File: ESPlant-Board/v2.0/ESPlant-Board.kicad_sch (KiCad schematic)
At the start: 32 parts, among them J1 Conn_02x04_Counter_Clockwise, U1 ESP32-S2-MINI-1-N4, U2 BH-AAA-B5AK001, U3 Reset, U4 Boot, U5 Temp/Humid-Sensor, U6 Light sensor, U7 AMS1117-3_3, U8 MK-12C02-G025

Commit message: Board: Update panel
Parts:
- removed J1: Conn_02x04_Counter_Clockwise, Connector_PinHeader_2.54mm:PinHeader_2x04_P2.54mm_Vertical, symbol Connector_Generic:Conn_02x04_Odd_Even
- removed R5: 10k, Resistor_SMD:R_0402_1005Metric, symbol Device:R
- removed R7: 1M, Resistor_SMD:R_0402_1005Metric, symbol Device:R
- removed U2: BH-AAA-B5AK001, CustomFootprints:BAT-SMD_BH-AAA-B5AA001, symbol Custom_Parts:BH-AAA-B5AK001
- added J1: Conn_01x05, Connector_PinHeader_2.54mm:PinHeader_1x05_P2.54mm_Vertical, symbol Connector_Generic:Conn_01x05
- added U9: ~, CustomFootprints:AAA Battery-spring, symbol Custom_Parts:AAA_Battery-Spring
- C3: value 1uF -> 150pF; LCSC C52923 -> C1527; MPN C52923 -> C1527
- USB1: now in the parts list
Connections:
- net Voltage_Measurement_Select_1 is gone; now on net TH_SCL: U1.35 (IO39)
- net +3V3: now also J1.5 (Pin_5)
- net GND: now also J1.1 (Pin_1), U9.1 (-)
- net IO0: now also J1.4 (Pin_4)
- net LED_GREEN: now also U1.38 (IO42); no longer U1.20 (IO16)
- net LED_RED: now also U1.37 (IO41); no longer U1.21 (IO17)
- net Light_Sensor_Analog: now also U1.7 (IO3); no longer U1.8 (IO4)
- net Light_Sensor_In: now also U1.36 (IO40); no longer U1.32 (IO36)
- net Light_Sensor_Select_1: now also U1.32 (IO36); no longer U1.33 (IO37)
- net RX: now also J1.2 (Pin_2)
- net Square_Wave_Signal: now also U1.21 (IO17); no longer U1.29 (IO34)
- net TH_SCL: no longer U1.38 (IO42)
- net TH_SDA: now also U1.34 (IO38); no longer U1.37 (IO41)
- net TX: now also J1.3 (Pin_3)
- net Voltage_Measurement_Analog: now also U1.10 (IO6); no longer U1.7 (IO3)
- net at U8.3: now also U9.2 (+)
- net IO2: no longer names the net of U1.6 (IO2)
- net Voltage_Measurement_Select_2 renamed Voltage_Measurement_Select
- net Voltage_Measurement_Select: now also U1.20 (IO16); no longer U1.34 (IO38)
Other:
- note removed: "10k is best for a ~6 Mhz Signal max(3.3*(1-e^(-(1/x)/(10000*7*10^-12))) -3.3*(1-e^(-(1/x)/(10000*47*10^-12)))) Expecting a sensor capacitance between 7 pF and 47 pF"
- moved on the sheet: R6

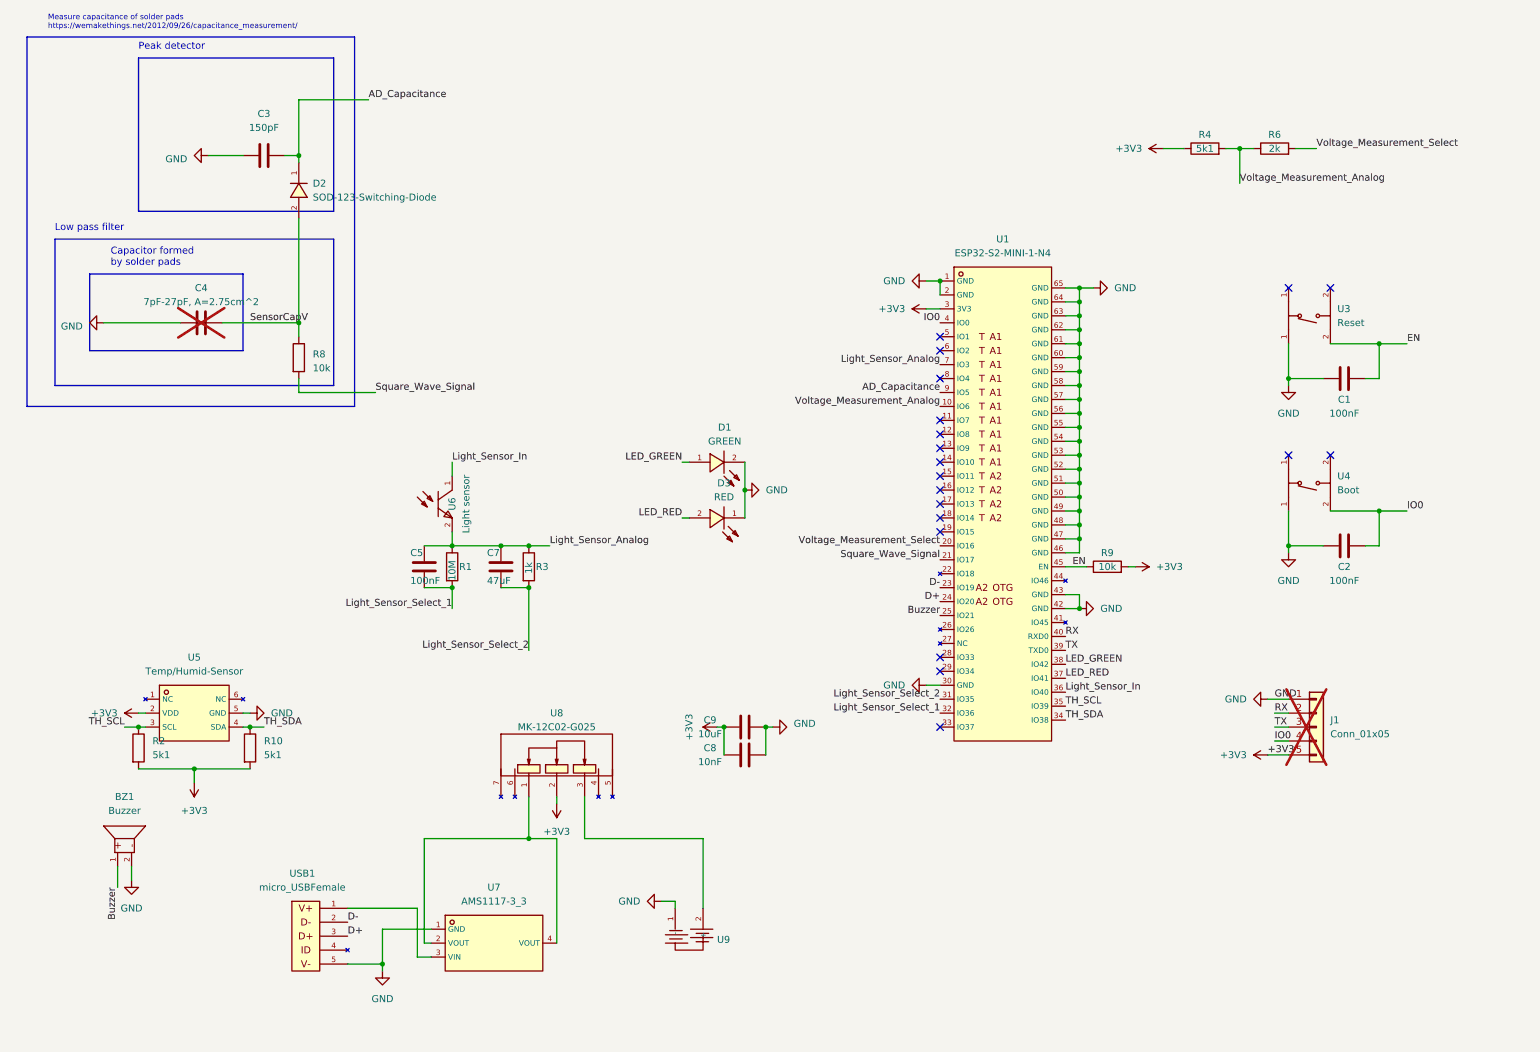
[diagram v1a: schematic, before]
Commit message: Board: Add panel for esp32-c6
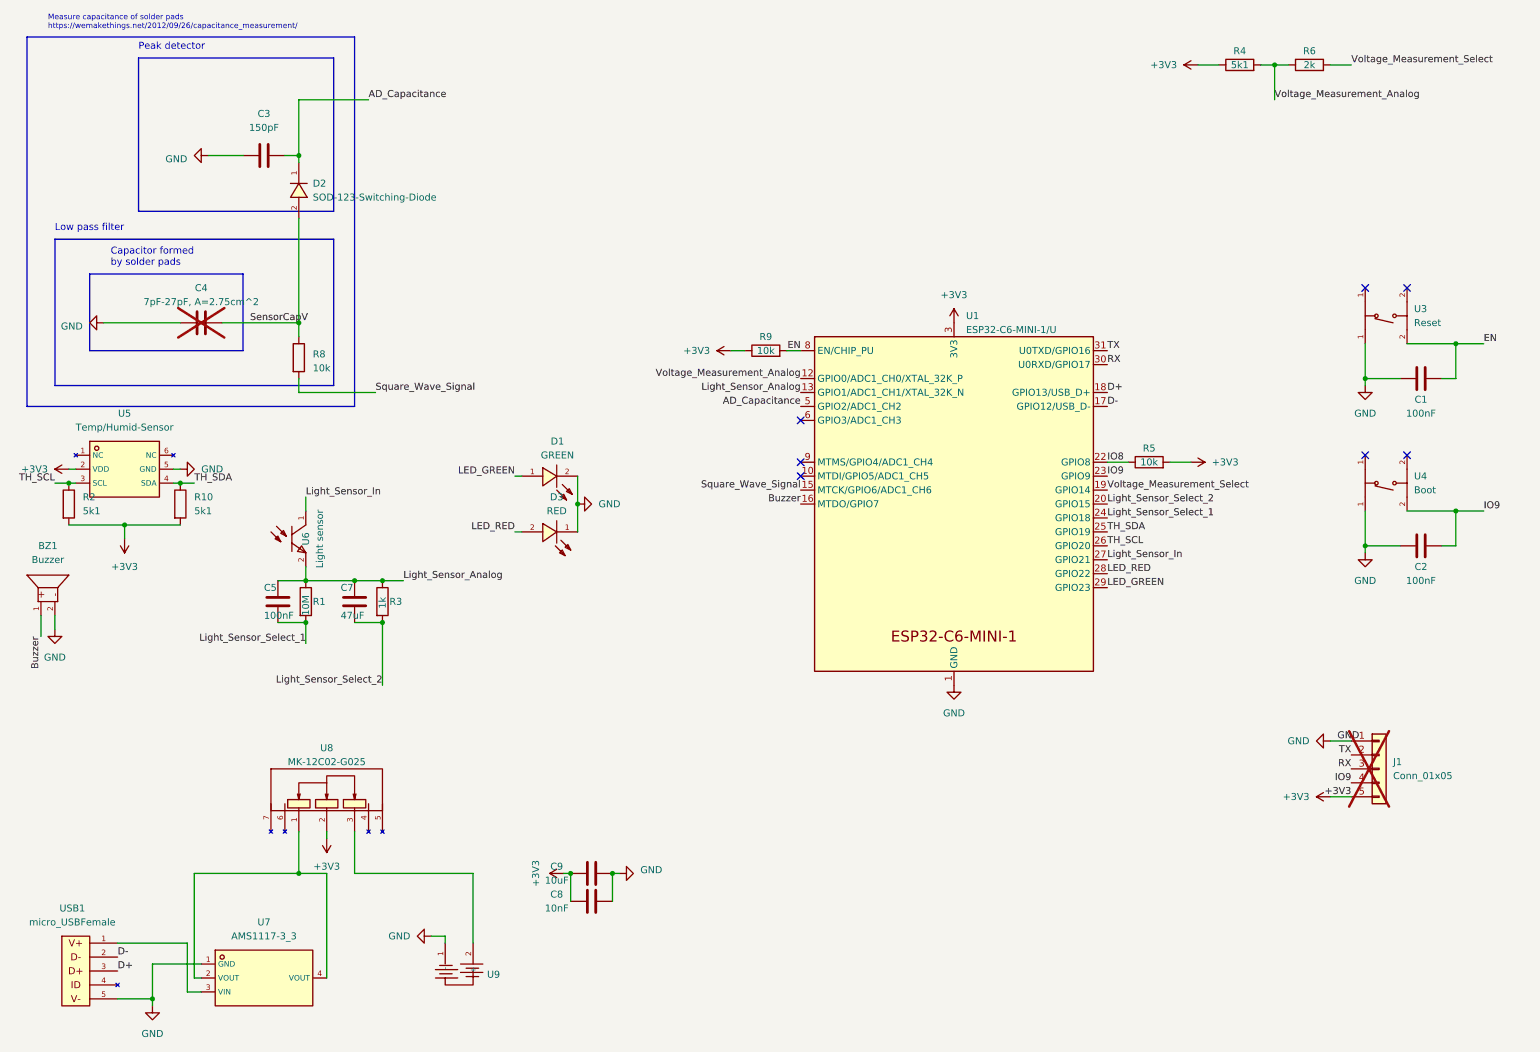
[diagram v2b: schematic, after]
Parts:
- removed U1: ESP32-S2-MINI-1-N4, CustomFootprints:WIFI-SMD_ESP32-MINI-1-N4, symbol Custom_Parts:ESP32-S2-MINI-1-N4
- added R5: 10k, Resistor_SMD:R_0402_1005Metric, symbol Device:R
- added U1: ESP32-C6-MINI-1/U, Espressif:ESP32-C6-MINI-1, symbol Espressif:ESP32-C6-MINI-1/U
- C4, J1, U9: LCSC (none) -> /; MPN (none) -> /
- U8: JLCPCB Position Offset (none) -> 0,0,-0.5
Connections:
- net IO0 is gone; now on net IO9: C2.2, J1.4 (Pin_4), U4.2 (D)
- net +3V3: now also R9.1, R5.2, U1.3 (3V3); no longer R9.2
- net AD_Capacitance: now also U1.5 (GPIO2/ADC1_CH2)
- net Buzzer: now also U1.16 (MTDO/GPIO7)
- net D+: now also U1.18 (GPIO13/USB_D+)
- net D-: now also U1.17 (GPIO12/USB_D-)
- net EN: now also R9.2, U1.8 (EN/CHIP_PU); no longer R9.1
- net GND: now also U1.1 (GND), U1.11 (GND), U1.14 (GND), U1.2 (GND), U1.36 (GND), U1.37 (GND), U1.38 (GND), U1.39 (GND), U1.40 (GND), U1.41 (GND), U1.42 (GND), U1.43 (GND), U1.44 (GND), U1.45 (GND), U1.46 (GND), U1.47 (GND), U1.48 (GND), U1.49 (GND), U1.50 (GND), U1.51 (GND), U1.52 (GND), U1.53 (GND)
- net LED_GREEN: now also U1.29 (GPIO23)
- net LED_RED: now also U1.28 (GPIO22)
- net Light_Sensor_Analog: now also U1.13 (GPIO1/ADC1_CH1/XTAL_32K_N)
- net Light_Sensor_In: now also U1.27 (GPIO21)
- net Light_Sensor_Select_1: now also U1.24 (GPIO18)
- net Light_Sensor_Select_2: now also U1.20 (GPIO15)
- net RX: now also J1.3 (Pin_3), U1.30 (U0RXD/GPIO17); no longer J1.2 (Pin_2)
- net Square_Wave_Signal: now also U1.15 (MTCK/GPIO6/ADC1_CH6)
- net TH_SCL: now also U1.26 (GPIO20)
- net TH_SDA: now also U1.25 (GPIO19)
- net TX: now also J1.2 (Pin_2), U1.31 (U0TXD/GPIO16); no longer J1.3 (Pin_3)
- net Voltage_Measurement_Analog: now also U1.12 (GPIO0/ADC1_CH0/XTAL_32K_P)
- net Voltage_Measurement_Select: now also U1.19 (GPIO14)
- net IO9: now reaches U4.2 (D)
- net IO9: now also U1.23 (GPIO9)
- new net IO8: R5.1, U1.22 (GPIO8)
- no-connect marks 19 -> 7
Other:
- moved on the sheet: BZ1, C1, C2, C5, C7, C8, C9, D1, D3, R1, R10, R2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
